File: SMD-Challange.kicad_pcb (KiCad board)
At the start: 2 copper layers, 40 x 40 mm, 20 parts, among them SW1 SW_DPDT_x2, U1 NE555, U2 4017

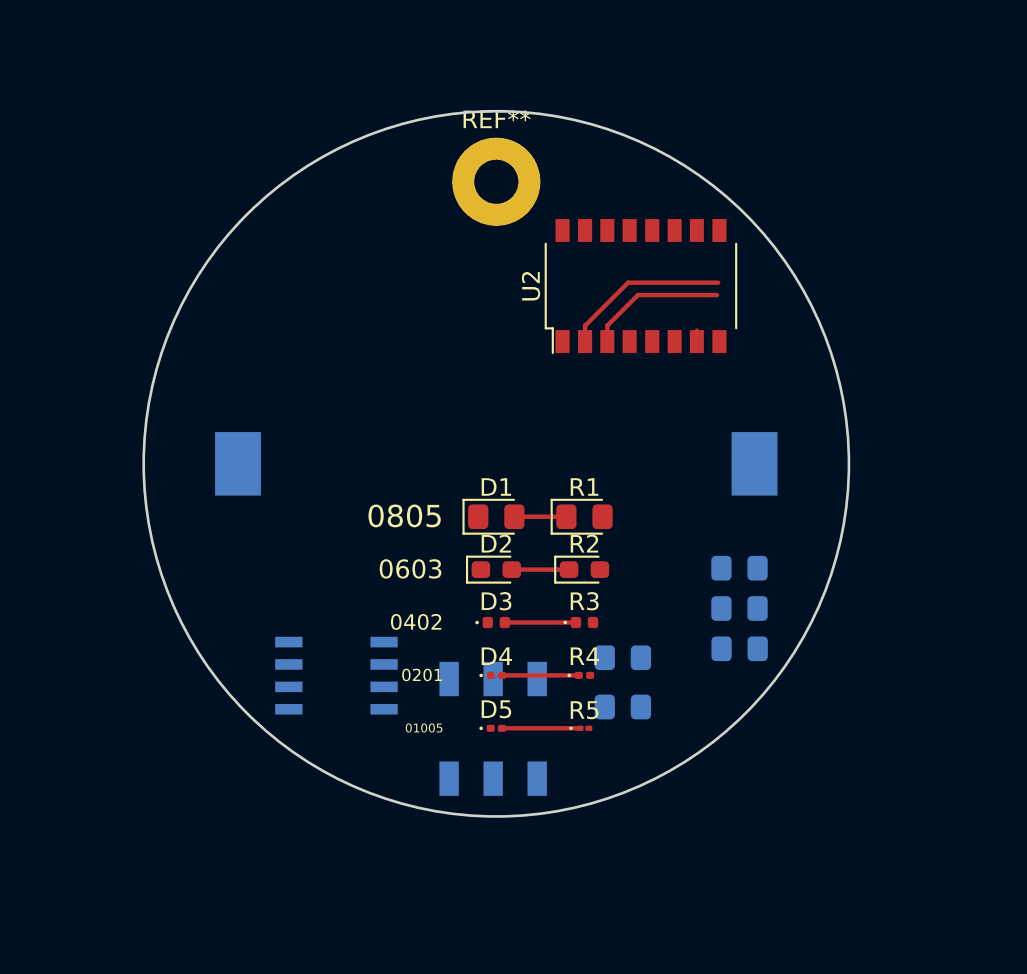
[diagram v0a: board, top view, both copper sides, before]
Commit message: managed to layout without visible via
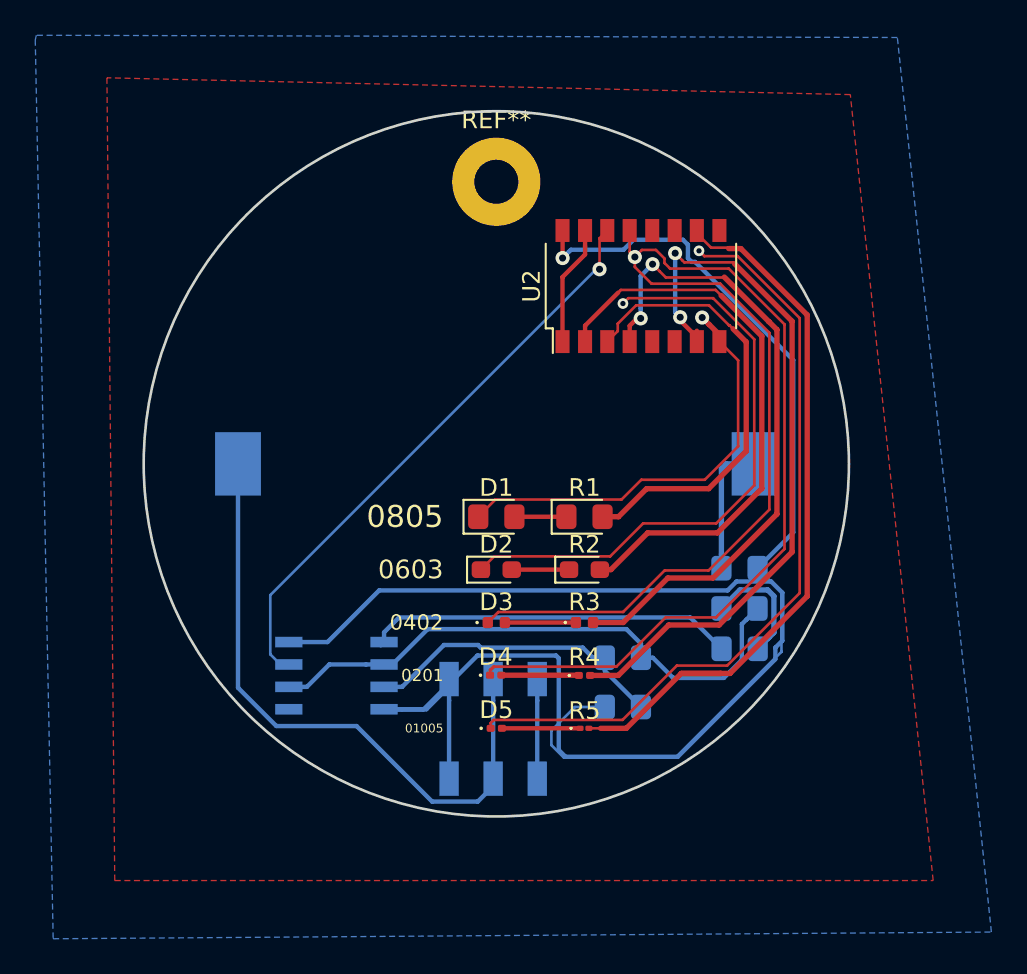
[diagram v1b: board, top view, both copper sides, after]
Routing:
- net GND: track 0.00 -> 201.4 mm, vias 0 -> 4
- net VS: track 0.00 -> 131.6 mm, vias 0 -> 1
- net Net-(R5-Pad2): track 0.00 -> 42.1 mm
- net Net-(R4-Pad2): track 0.62 -> 41.8 mm, vias 0 -> 2
- net Net-(R3-Pad2): track 0.00 -> 37.0 mm, vias 0 -> 2
- net +3V3: track 0.00 -> 36.3 mm
- net Net-(U1-Pad3): track 0.00 -> 33.4 mm, vias 0 -> 1
- net Net-(C2-Pad2): track 0.00 -> 32.4 mm
- net Net-(R2-Pad2): track 9.46 -> 32.6 mm
- net Net-(C3-Pad1): track 0.00 -> 21.1 mm
- net Net-(R1-Pad2): track 7.85 -> 25.7 mm
- net Net-(R6-Pad2): track 0.00 -> 17.4 mm
- net Net-(U2-Pad1): track 0.00 -> 6.83 mm
- net Net-(SW1-Pad3): track 0.00 -> 5.65 mm
- added copper zone on B.Cu, net GND
- added copper zone on F.Cu, net VS

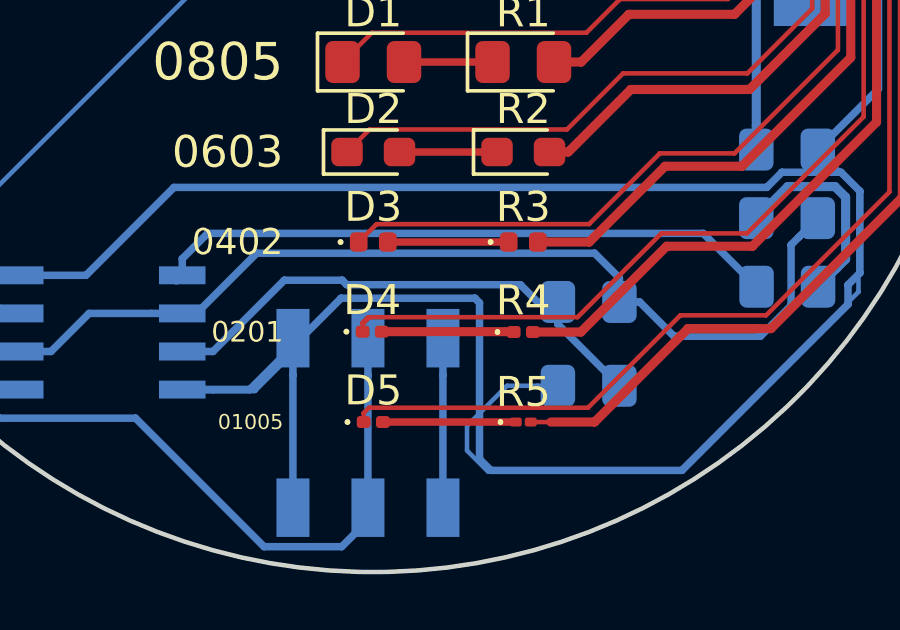
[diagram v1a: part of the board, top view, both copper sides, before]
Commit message: added custom footprints for smd 0201 and 01005 for hand-soldering
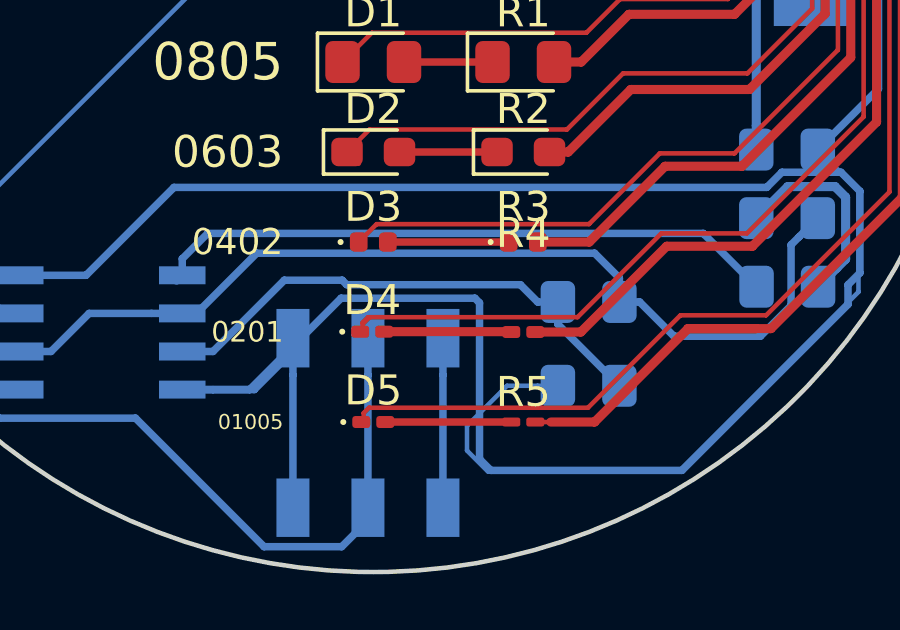
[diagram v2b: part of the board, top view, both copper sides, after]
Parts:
- BT1: value Battery_Cell -> CR2023
- C1, C3: value C -> 100n
- C2: value C -> 1µ
- D4, D5: footprint LED_SMD:LED_0201_0603Metric -> SMD-Challange:LED_0201_0603Metric_hand_soldering
- R4: footprint LED_SMD:LED_0201_0603Metric -> SMD-Challange:R_0201_0603Metric_hand_soldering
- R5: footprint LED_SMD:LED_01005_0402Metric -> SMD-Challange:R_01005_0402Metric_hand_soldering
- R6, R7: value R -> 100k

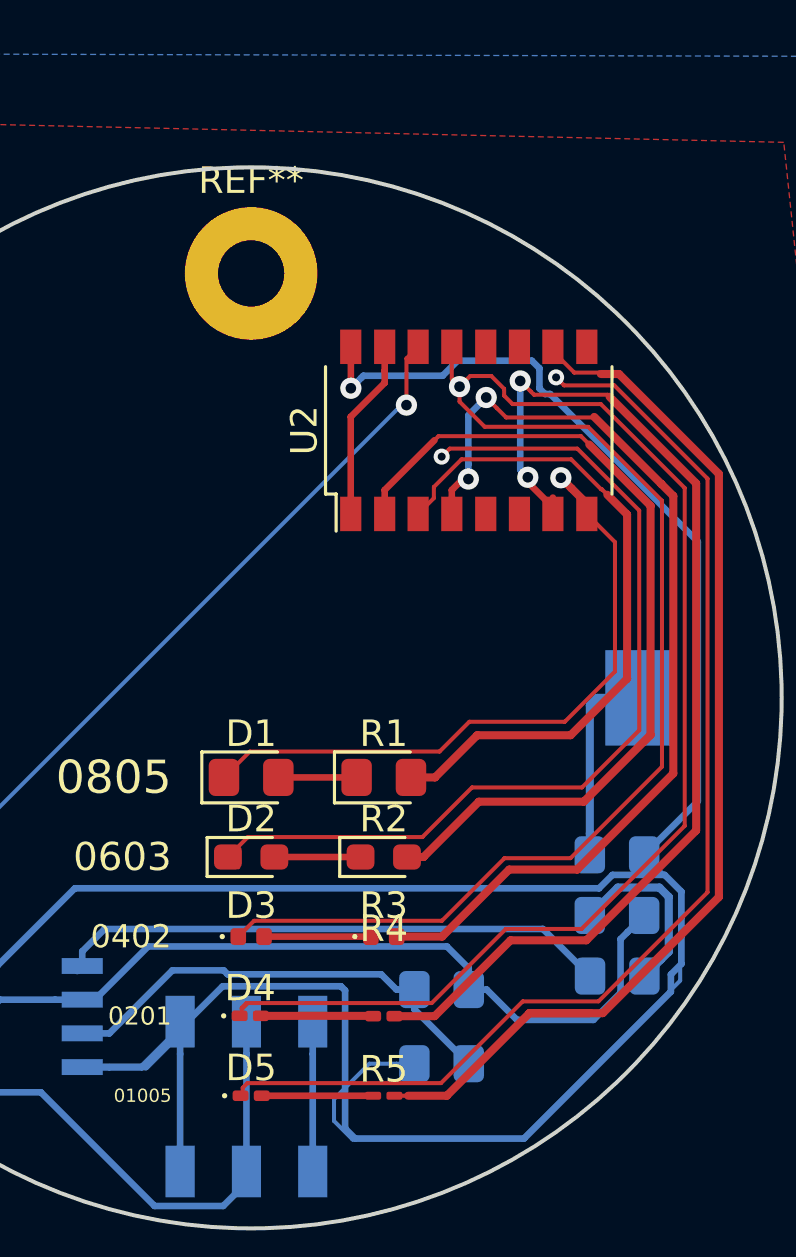
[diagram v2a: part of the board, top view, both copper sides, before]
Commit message: changed some footprints and made the surface printing nicer
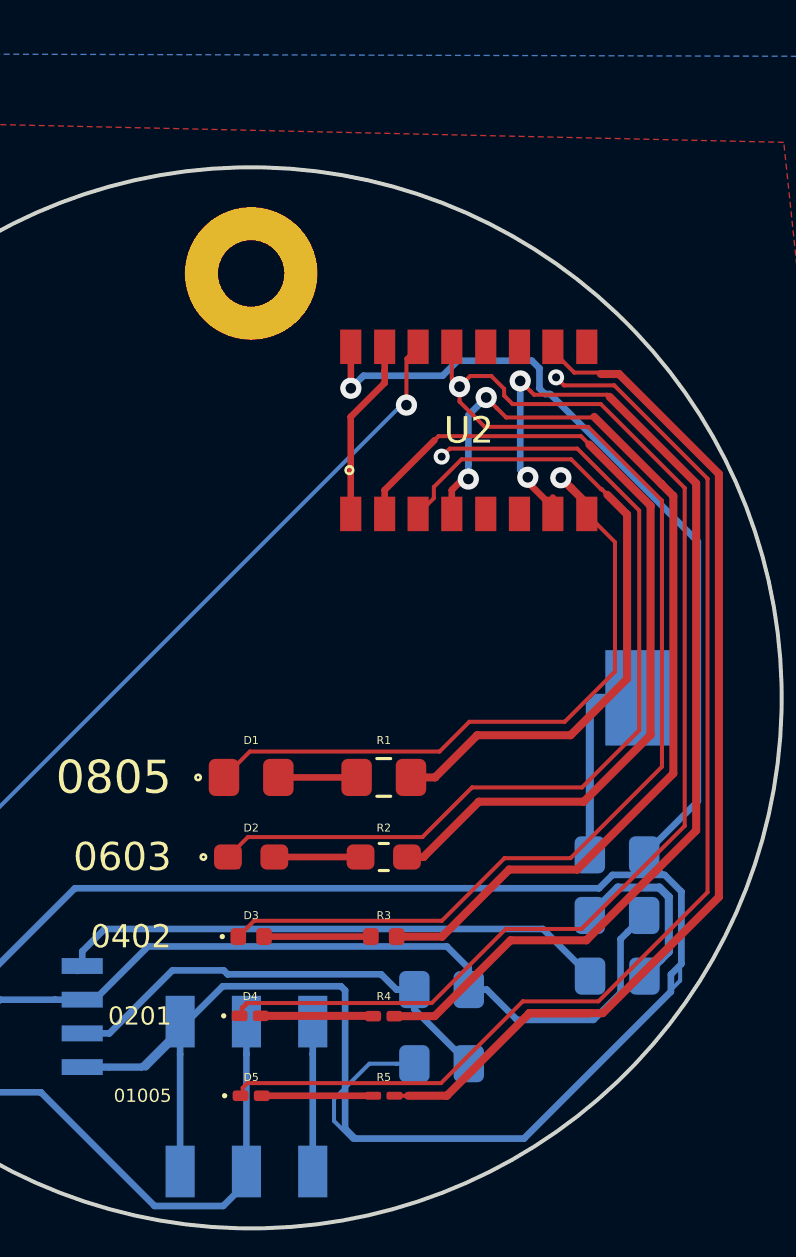
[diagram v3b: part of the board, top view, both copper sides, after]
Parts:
- D1: footprint LED_SMD:LED_0805_2012Metric_Pad1.15x1.40mm_HandSolder -> SMD-Challange:LED_0805_2012Metric_Pad1.15x1.40mm_HandSolder_simple_drawing
- D2: footprint LED_SMD:LED_0603_1608Metric_Pad1.05x0.95mm_HandSolder -> SMD-Challange:LED_0603_1608Metric_Pad1.05x0.95mm_HandSolder_simple_drawing
- R1: footprint LED_SMD:LED_0805_2012Metric_Pad1.15x1.40mm_HandSolder -> Resistor_SMD:R_0805_2012Metric_Pad1.15x1.40mm_HandSolder
- R2: footprint LED_SMD:LED_0603_1608Metric_Pad1.05x0.95mm_HandSolder -> Resistor_SMD:R_0603_1608Metric_Pad1.05x0.95mm_HandSolder
- R3: footprint LED_SMD:LED_0402_1005Metric -> Resistor_SMD:R_0402_1005Metric
- U2: footprint Package_SO:SOP-16_4.4x10.4mm_P1.27mm -> SMD-Challange:SOP-16_4.4x10.4mm_P1.27mm_simple_drawing
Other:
- board text added: "CC-BY-SA 3.0"
- board text added: "binary-kitchen.de"
